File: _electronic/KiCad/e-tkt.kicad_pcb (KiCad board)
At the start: 2 copper layers, 99.6 x 76.2 mm, 130 parts

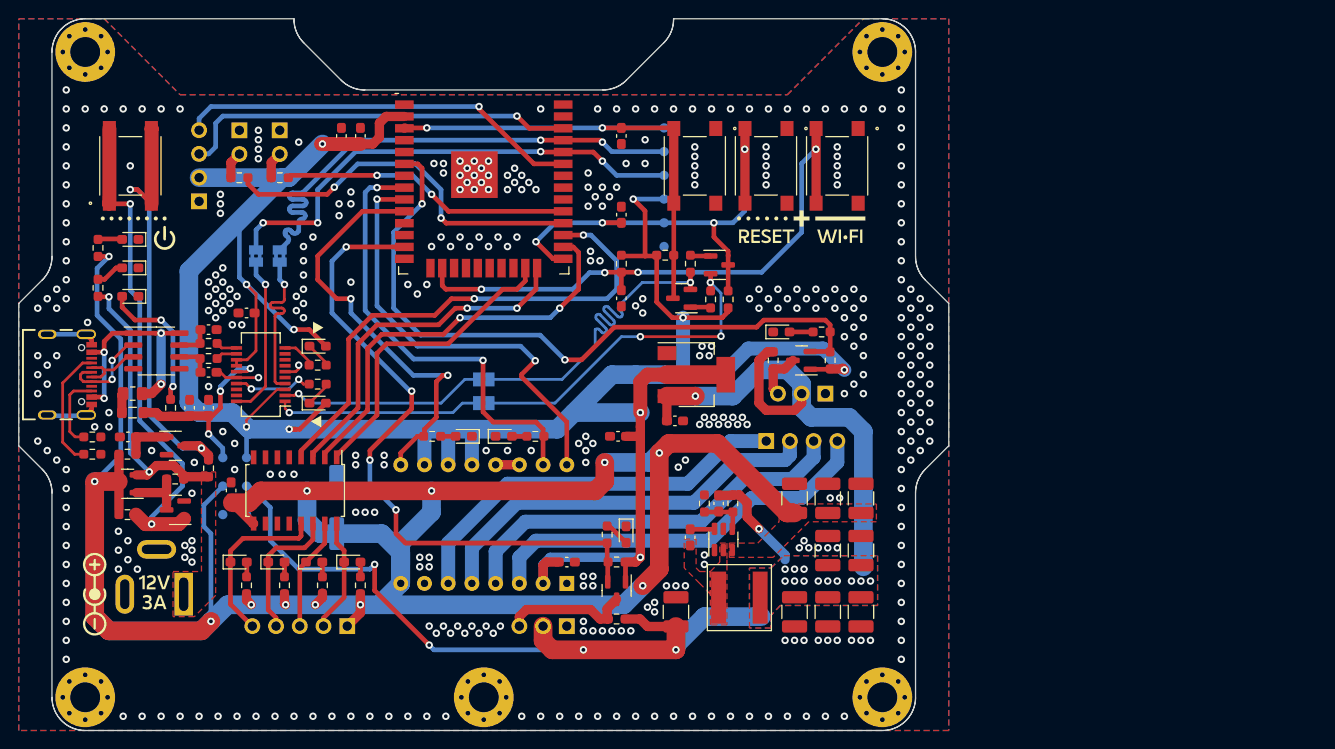
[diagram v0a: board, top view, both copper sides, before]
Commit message: hierarchical sheets and overall organization
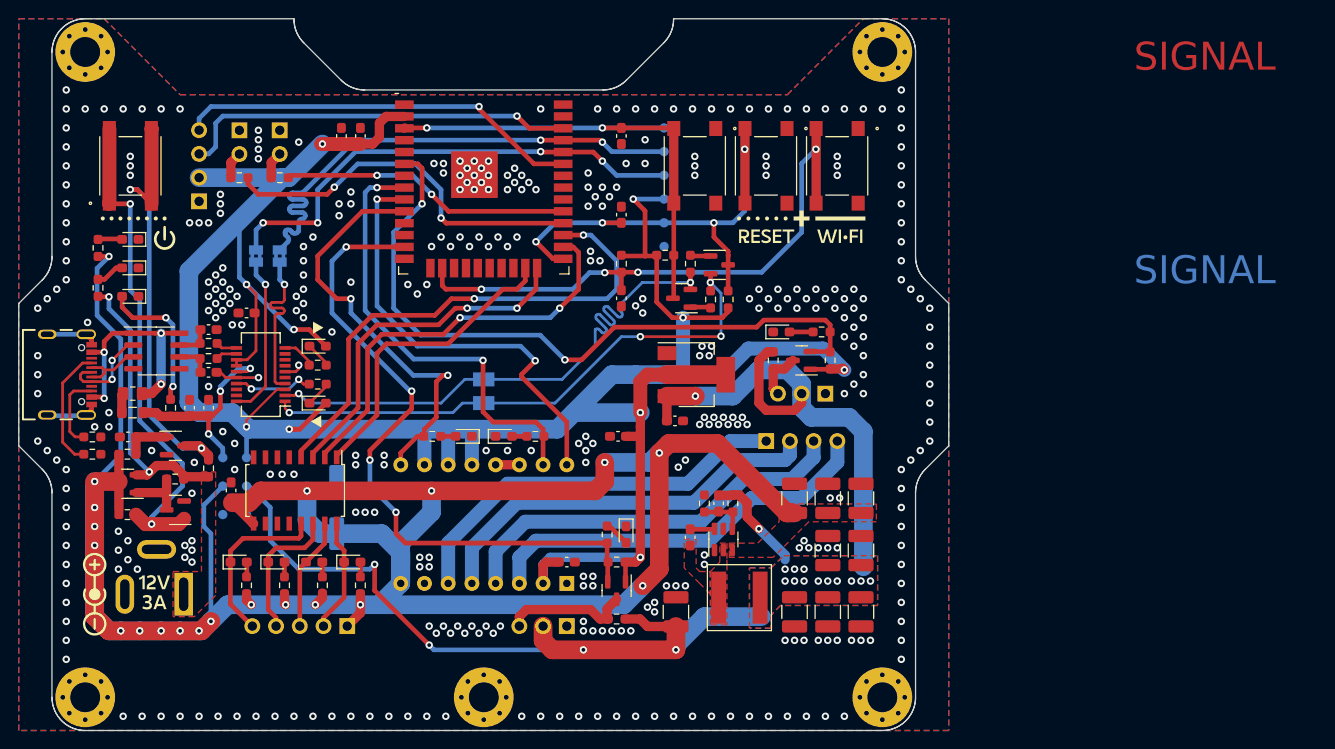
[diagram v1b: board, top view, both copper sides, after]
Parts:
- removed REF**: OSHW-Symbol_6.7x6mm_SilkScreen, Symbol:OSHW-Symbol_6.7x6mm_SilkScreen
- C_POW_6V_FF1: value 82pF 6V 0Ohm -> 82pF 100V
- C_POW_BST1: value 100nF 6V 64mOhm -> 0.1uF 50V
- C_POW_IN1, C_POW_IN2, C_POW_IN3: value 10uF 12V 5mOhm -> 10uF 25V
- C_POW_OUT1, C_POW_OUT2, C_POW_OUT3, C_POW_OUT4, C_POW_OUT5: value 22uF 12V 1mOhm -> 22uF 25V
- J_POW1: footprint SnapEDA Library:BarrelJack_GCT_DCJ200-10-A_Horizontal -> Connector_BarrelJack:BarrelJack_GCT_DCJ200-10-A_Horizontal
- L1: value 11uH/15.8mOhm1 -> ~
- U_POW1: value TPS54302 -> ~
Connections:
- net /POWER IN renamed Net-(J_POW1-Pad1)
- net /USBD1+ renamed /USB-C 2.0/USBD1+
- net /USBD1- renamed /USB-C 2.0/USBD1-
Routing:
- net GNDREF: vias 401 -> 372
- net +12V: vias 12 -> 20
- added copper zone on In3.Cu, net +12V
- added copper zone on In2.Cu, net +6V
- added copper zone on In1.Cu, net GNDREF
- added copper zone on In4.Cu, net GNDREF
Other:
- copper layers 2 -> 6
- board text added: "12V"
- board text added: "6V"
- board text added: "SIGNAL"

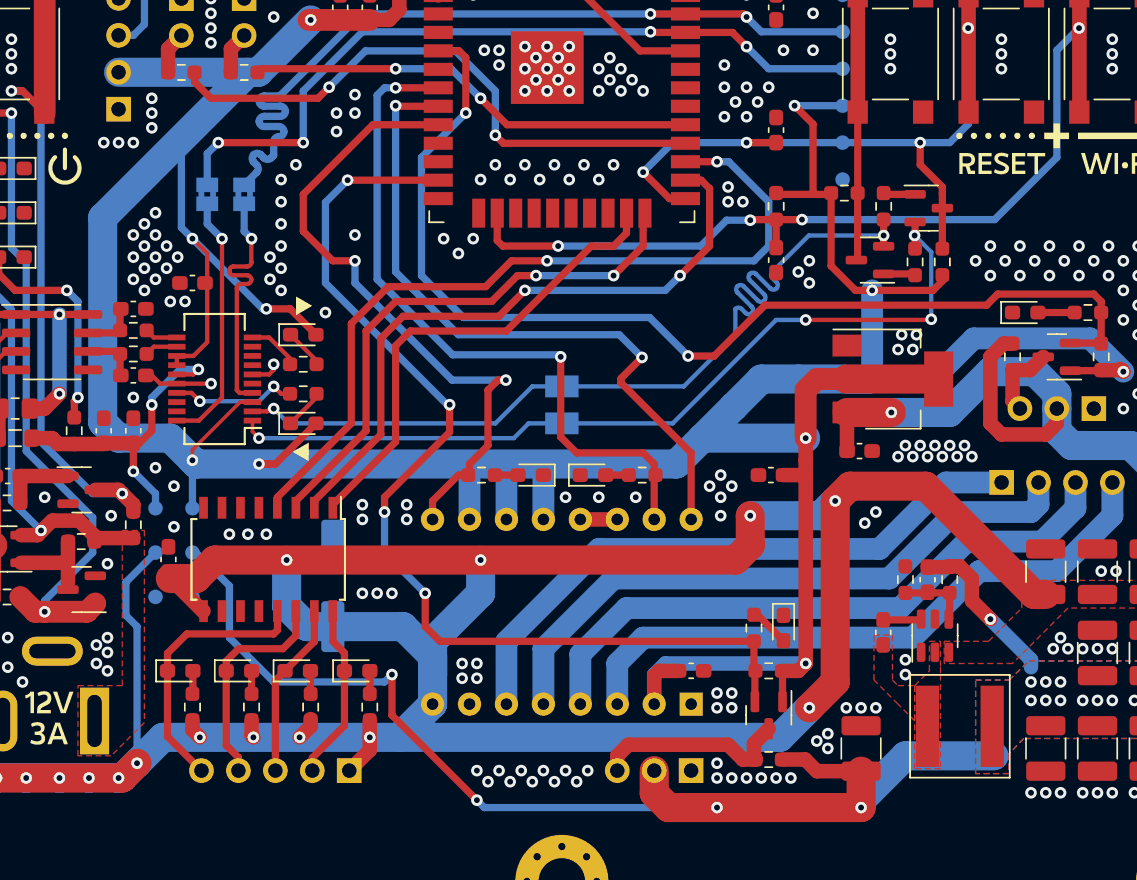
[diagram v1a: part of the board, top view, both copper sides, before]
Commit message: added buzzer
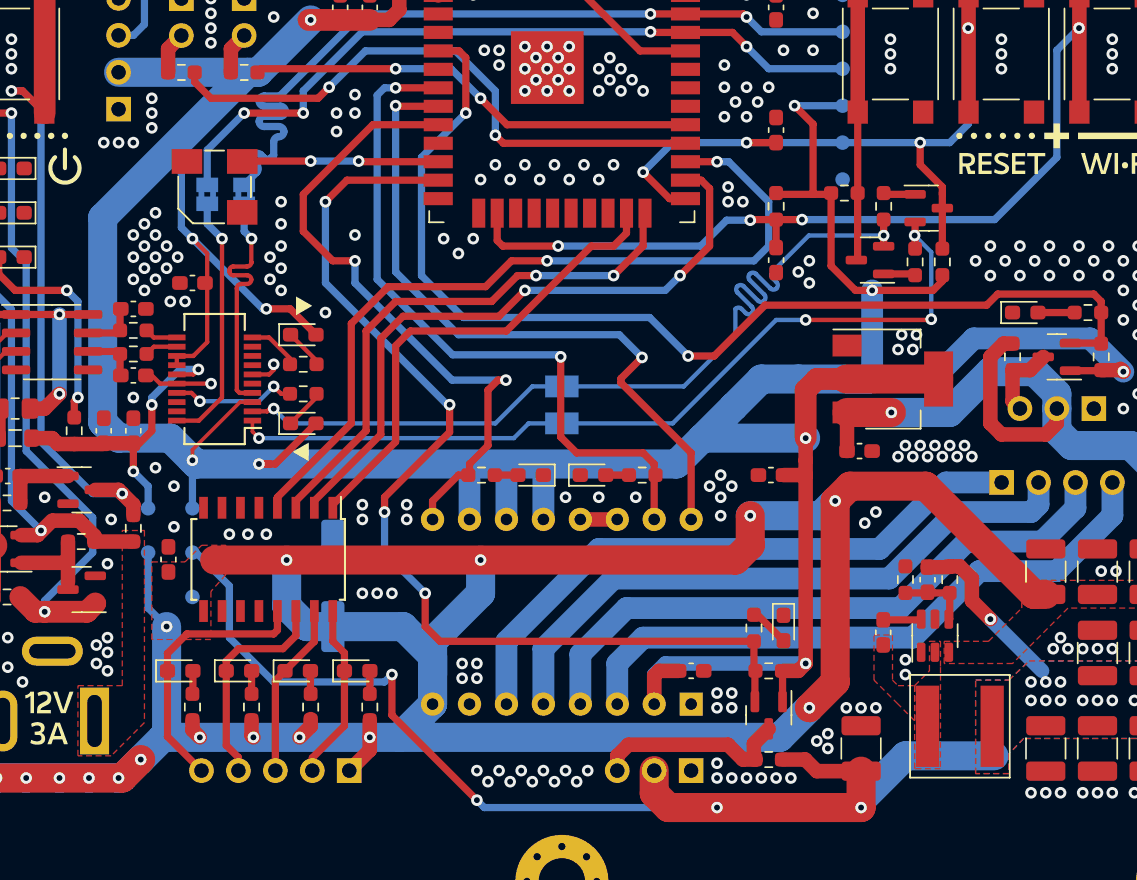
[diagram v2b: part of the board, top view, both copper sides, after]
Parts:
- removed TP_GND2: TestPoint, TestPoint:TestPoint_Pad_D1.0mm
- added LS1: CSS-0575A-SMT, SnapEDA Library:CUI_CSS-0575A-SMT, F.Cu at (154.4, -202.7)
- moved TP_12v1 0.51 mm to (149.9, -177.6)
- moved TP_5v1 0.51 mm to (149.9, -180.6)
- moved R_POW5 0.24 mm to (148.8, -179.2)
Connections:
- U_MCU1 pad 12: unconnected-(U_MCU1-Pad12) -> /MCU/IO27 BUZZER OUT
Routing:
- net /MCU/IO27 BUZZER OUT: track 0.00 -> 13.5 mm, vias 0 -> 2
- net +12V: track 284.2 -> 274.2 mm, vias 20 -> 21
- net IO3 RXD: track 52.4 -> 51.4 mm
- net +6V: track 150.2 -> 150.8 mm
- net GNDREF: vias 372 -> 370

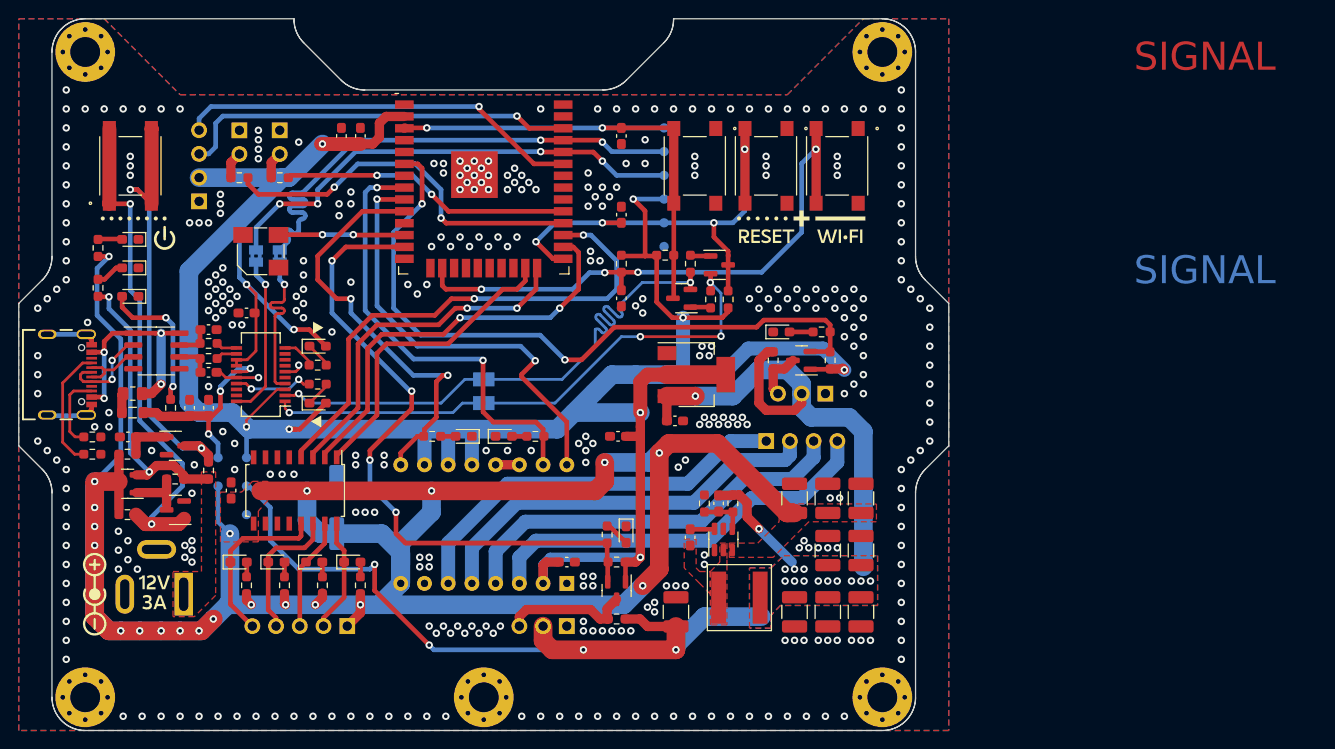
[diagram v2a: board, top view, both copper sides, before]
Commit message: external flashing header
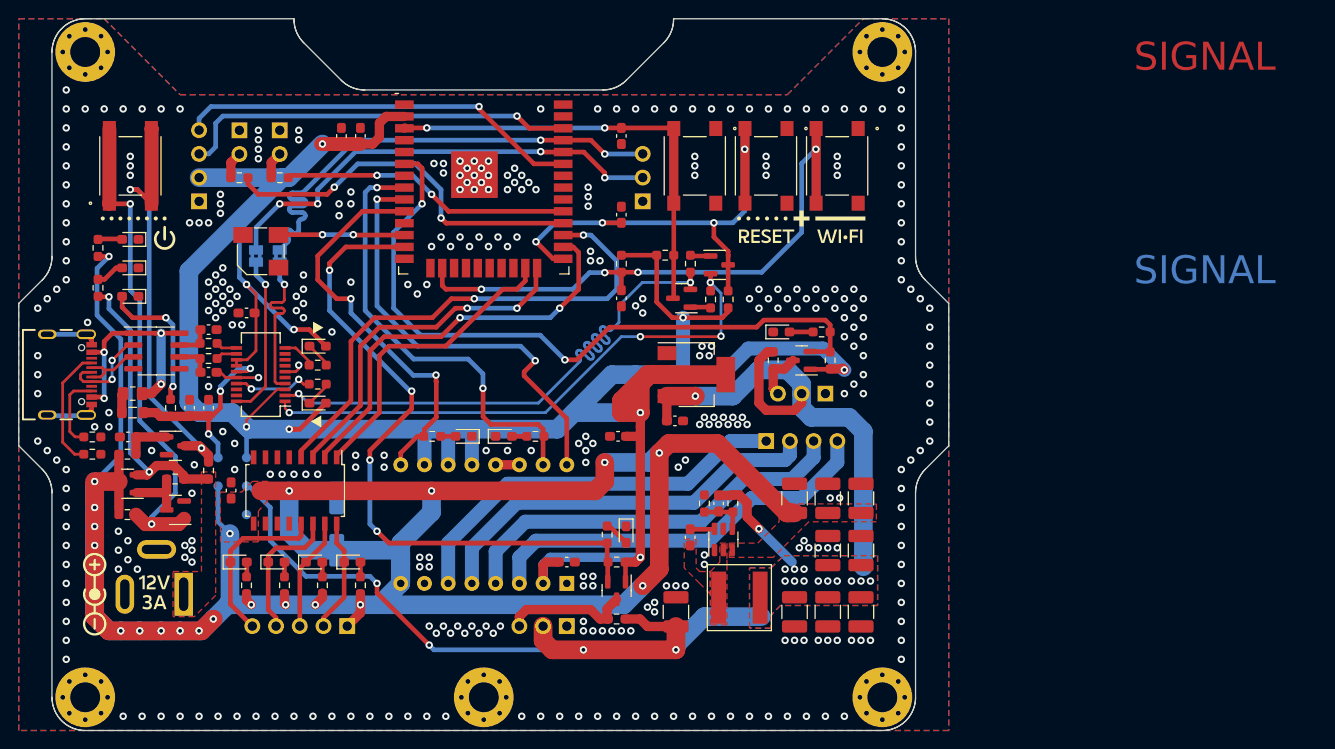
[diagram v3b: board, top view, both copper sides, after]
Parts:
- removed JP_SER2, JP_SER4: Bridged, Jumper:SolderJumper-2_P1.3mm_Bridged2Bar_Pad1.0x1.5mm
- removed TP_CTS1, TP_DTR1, TP_GND1, TP_RX1, TP_TX1, TP_VCC_3.3V1: TestPoint, TestPoint:TestPoint_Pad_D1.0mm
- added J_EXT1: Conn_01x03_Male, Connector_PinHeader_2.54mm:PinHeader_1x03_P2.54mm_Horizontal, B.Cu at (195.3, -208.0)
- J_POW1: footprint Connector_BarrelJack:BarrelJack_GCT_DCJ200-10-A_Horizontal -> SnapEDA Library:BarrelJack_GCT_DCJ200-10-A_Horizontal
- moved C_NEMA1 1.78 mm to (162.6, -173.5)
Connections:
- U_SER1 pad 1: Net-(JP_SER2-Pad1) -> DTR
- U_SER1 pad 2: Net-(JP_SER4-Pad1) -> RTS
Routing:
- net RTS: track 37.1 -> 62.5 mm, vias 1 -> 2
- net DTR: track 35.9 -> 59.2 mm, vias 3 -> 4
- net Net-(JP_SER4-Pad1): track 22.2 -> 0.00 mm, vias 1 -> 0
- net Net-(JP_SER2-Pad1): track 22.0 -> 0.00 mm, vias 1 -> 0
- net EN: track 53.8 -> 47.2 mm
- net +12V: track 274.2 -> 276.9 mm
- net IO1 TXD: track 55.8 -> 53.6 mm
- net IO25 NEMA ENA: track 45.2 -> 43.2 mm
- net IO3 RXD: track 51.4 -> 49.5 mm
- net +6V: track 150.8 -> 149.3 mm
- net IO14 SERVO: track 71.7 -> 72.9 mm
- net Net-(Q_POW3-Pad3): track 47.2 -> 46.0 mm
- net Net-(Q_POW2-Pad1): track 54.2 -> 53.5 mm
- net IO32 NEMA STEP: track 48.4 -> 47.9 mm
- net +3.3V: track 280.1 -> 279.9 mm, vias 10 -> 9
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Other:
- board text added: "END"
- board text added: "EXTERNAL ! 3V3 ! FLASHING"
- board text added: "LEDS"
- board text added: "PRESS"
- board text added: "RX EXT"
- board text added: "TX EXT"
- board text removed: "CTS"
- board text removed: "CUT"
- board text removed: "DTR"
- board text removed: "EXTERNAL FLASHING"
- board text removed: "LED END"
- board text removed: "LED PRESS"
- board text removed: "RX"
- board text removed: "TX"
- board text removed: "VCC 3.3v"
